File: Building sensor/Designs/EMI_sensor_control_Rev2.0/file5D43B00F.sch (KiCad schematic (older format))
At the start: 45 parts, among them U14 AD8021ARZ, U15 AD7763BSVZ

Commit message: overdue backup
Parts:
- removed C44, C52, C53, C54, C55, C56, C57, C58, C60, C61: C 100n, Capacitor_SMD:C_0603_1608Metric_Pad1.05x0.95mm_HandSolder, symbol Device:C
- removed C45: C 33p, Capacitor_SMD:C_0402_1005Metric, symbol Device:C
- removed C46: C 100u, Capacitor_Tantalum_SMD:CP_EIA-7343-30_AVX-N_Pad2.25x2.55mm_HandSolder, symbol Device:C
- removed C48, C59: C 10n, Capacitor_SMD:C_0805_2012Metric_Pad1.15x1.40mm_HandSolder, symbol Device:C
- removed FB11, FB12, FB13, FB14, FB15, FB16, FB17, FB18, FB19, FB20: Ferrite_Bead, Capacitor_SMD:C_0603_1608Metric_Pad1.05x0.95mm_HandSolder, symbol Device:Ferrite_Bead
- removed L6: L 8.2n, Inductor_SMD:L_0603_1608Metric_Pad1.05x0.95mm_HandSolder, symbol Device:L
- removed R49: R 10k, Resistor_SMD:R_1206_3216Metric_Pad1.42x1.75mm_HandSolder, symbol Device:R
- removed R51: R 100, Resistor_SMD:R_1206_3216Metric_Pad1.42x1.75mm_HandSolder, symbol Device:R
- removed R52: R 160k, Resistor_SMD:R_1206_3216Metric_Pad1.42x1.75mm_HandSolder, symbol Device:R
- removed R53, R61: R 10, Resistor_SMD:R_1206_3216Metric_Pad1.42x1.75mm_HandSolder, symbol Device:R
- removed R55, R56: R 18, Resistor_SMD:R_0805_2012Metric_Pad1.15x1.40mm_HandSolder, symbol Device:R
- removed U15: AD7763BSVZ, footprints:AD7763BSVZ, symbol 2019-07-11_15-43-26:AD7763BSVZ
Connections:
- net labels removed: +2V5, ADCReset, ADCSync, ADR0r, ADR1r, ADR2r, AGND1r, AGND2r, AGND3r, AGND4r, DRDY, FSI, FSOr, GNDD, GNDREF, GNDS, MCLK, Pin12r, Pin14r, Pin15r, Pin24r, Pin27r, Pin33r, Pin41r, Pin44r, Pin4r, Pin63r, Pin6r, SCO, SDI, SDLr, SDO, SH0r, SH1, SH2, Vref4.1
- wire segments 264 -> 51

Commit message: backup
2/04/2020
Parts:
- added C? (x7): C 1u, Capacitor_SMD:C_0402_1005Metric, symbol Device:C
- added R? (x3): R 100k, Resistor_SMD:R_0805_2012Metric_Pad1.15x1.40mm_HandSolder, symbol Device:R
- added R?: R 10k, Resistor_SMD:R_0805_2012Metric_Pad1.15x1.40mm_HandSolder, symbol Device:R
- added R?: R 60.4k, Resistor_SMD:R_0805_2012Metric_Pad1.15x1.40mm_HandSolder, symbol Device:R
- added U?: ADS127L01IPBSR, PBS0032A_N, symbol 2019-12-03_16-41-56:ADS127L01IPBSR
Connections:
- net GND: now also C?.1, C?.1, C?.1, C?.1, C?.1, C?.1, C?.2, R?.1, R?.1, R?.2, R?.2, U?.26 (DGND), U?.32 (AVDD), U?.5 (AGND)
- new net: C?.1, U?.1 (LVDD)
- new net: C?.2, U?.11 (CAP2)
- new net: R?.1, U?.14 (FSMODE)
- new net: C?.2, U?.2 (CAP1)
- new net: C?.2, U?.25 (CAP3)
- new net: R?.1, U?.29 (HR)
- new net: R?.1, U?.30 (FORMAT)
- new net: R?.2, U?.7 (REXT)
- new net: R?.2, U?.8 (INTLDO_N)
- new net +3V0: C?.2, C?.2, U?.27 (DVDD), U?.31 (AGND)
- new net +3V3: C?.2, R?.2, U?.6 (AVDD)
- new net Rx_CS: U?.19 (DRDY_FSYNC_N)
- new net Rx_Clk: U?.22 (SCLK)
- new net Rx_FIL0: U?.13 (FILTER0)
- new net Rx_FIL1: U?.12 (FILTER1)
- new net Rx_MISO: U?.20 (DOUT)
- new net Rx_MOSI: U?.21 (DIN)
- new net Rx_OSR0: U?.16 (OSR0)
- new net Rx_OSR1: U?.15 (OSR1)

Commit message: Back up
Backup of rev 2.0 for board
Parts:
- removed C49: C 5.6p, Capacitor_SMD:C_0402_1005Metric, symbol Device:C
- removed C50, C51: C 33p, Capacitor_SMD:C_0402_1005Metric, symbol Device:C
- removed R57, R58: R 1k, Resistor_SMD:R_0805_2012Metric_Pad1.15x1.40mm_HandSolder, symbol Device:R
- removed R59, R60: R 649, Resistor_SMD:R_0805_2012Metric_Pad1.15x1.40mm_HandSolder, symbol Device:R
- added R? (x2): R 1k, Resistor_SMD:R_0805_2012Metric_Pad1.15x1.40mm_HandSolder, symbol Device:R
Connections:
- net ADC_Reset: now also U?.28 (RESET_PWDN_N)
- net RxFiltered: now also R?.2
- net Rx_START: now also U?.17 (START)
- net -RxFiltered: now reaches R54.1, U14.6 (VOUT)
- net -RxFiltered: now also R?.2
- net at U?.3 (AINN): now also R?.1
- net at U?.4 (AINP): now also R?.1
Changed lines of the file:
@@
 $EndDescr
-$Comp
-L Device:R R58
-U 1 1 5D456184
-P 6350 9850
-AR Path="/5D3E2E6F/5D43B010/5D456184" Ref="R58"  Part="1"
-AR Path="/5DB20FE4/5D456184" Ref="R?"  Part="1"
-F 0 "R58" V 6350 9850 50  0000 C CNN
-F 1 "R 1k" V 6234 9850 50  0000 C CNN
-F 2 "Resistor_SMD:R_0805_2012Metric_Pad1.15x1.40mm_HandSolder" V 6280 9850 50  0001 C CNN
-F 3 "~" H 6350 9850 50  0001 C CNN
-	1    6350 9850
-	0    1    1    0
-$EndComp
 $Comp
 L Device:R R48
@@
 	5800 9650 5800 9550
 Connection ~ 5800 9650
-$Comp
-L Device:C C49
-U 1 1 5D4561C9
-P 6750 9650
-AR Path="/5D3E2E6F/5D43B010/5D4561C9" Ref="C49"  Part="1"
-AR Path="/5DB20FE4/5D4561C9" Ref="C?"  Part="1"
-F 0 "C49" H 6865 9696 50  0000 L CNN
-F 1 "C 5.6p" H 6800 9550 50  0000 L CNN
-F 2 "Capacitor_SMD:C_0402_1005Metric" H 6788 9500 50  0001 C CNN
-F 3 "~" H 6750 9650 50  0001 C CNN
-	1    6750 9650
-	1    0    0    -1
-$EndComp
-Wire Wire Line
-	6750 9500 6750 9450
-$Comp
-L Device:R R57
-U 1 1 5D4561D0
-P 6350 9450
-AR Path="/5D3E2E6F/5D43B010/5D4561D0" Ref="R57"  Part="1"
-AR Path="/5DB20FE4/5D4561D0" Ref="R?"  Part="1"
-F 0 "R57" V 6350 9450 50  0000 C CNN
-F 1 "R 1k" V 6234 9450 50  0000 C CNN
-F 2 "Resistor_SMD:R_0805_2012Metric_Pad1.15x1.40mm_HandSolder" V 6280 9450 50  0001 C CNN
-F 3 "~" H 6350 9450 50  0001 C CNN
-	1    6350 9450
-	0    1    1    0
-$EndComp
-Wire Wire Line
-	6500 9850 6750 9850
-Wire Wire Line
-	6500 9450 6750 9450
-Wire Wire Line
-	6750 9850 6750 9800
-Text GLabel 7100 9850 2    50   Input ~ 0
-Pin20r
-Text GLabel 7100 9450 2    50   Input ~ 0
-Pin19r
-Wire Wire Line
-	6750 9850 7100 9850
-Connection ~ 6750 9850
-Wire Wire Line
-	6750 9450 7100 9450
-Connection ~ 6750 9450
-Text GLabel 7700 10000 2    50   Input ~ 0
-Pin22r+
-Text GLabel 7700 9300 2    50   Input ~ 0
-Pin21r-
-Connection ~ 5950 9850
-Wire Wire Line
-	5950 9850 6200 9850
 Wire Wire Line
 	4600 9150 5950 9150
-$Comp
-L Device:R R59
-U 1 1 5D4561F0
-P 7050 9200
-AR Path="/5D3E2E6F/5D43B010/5D4561F0" Ref="R59"  Part="1"
-AR Path="/5DB20FE4/5D4561F0" Ref="R?"  Part="1"
-F 0 "R59" V 7050 9200 50  0000 C CNN
-F 1 "R 649" V 6934 9200 50  0000 C CNN
-F 2 "Resistor_SMD:R_0805_2012Metric_Pad1.15x1.40mm_HandSolder" V 6980 9200 50  0001 C CNN
-F 3 "~" H 7050 9200 50  0001 C CNN
-	1    7050 9200
-	0    1    1    0
-$EndComp
-$Comp
-L Device:C C51
-U 1 1 5D4561F6
-P 7050 10350
-AR Path="/5D3E2E6F/5D43B010/5D4561F6" Ref="C51"  Part="1"
-AR Path="/5DB20FE4/5D4561F6" Ref="C?"  Part="1"
-F 0 "C51" V 7300 10300 50  0000 L CNN
-F 1 "C 33p" V 7200 10200 50  0000 L CNN
-F 2 "Capacitor_SMD:C_0402_1005Metric" H 7088 10200 50  0001 C CNN
-F 3 "~" H 7050 10350 50  0001 C CNN
-	1    7050 10350
-	0    1    1    0
-$EndComp
-$Comp
-L Device:C C50
-U 1 1 5D4561FC
-P 7050 8850
-AR Path="/5D3E2E6F/5D43B010/5D4561FC" Ref="C50"  Part="1"
-AR Path="/5DB20FE4/5D4561FC" Ref="C?"  Part="1"
-F 0 "C50" V 6800 8800 50  0000 L CNN
-F 1 "C 33p" V 6900 8750 50  0000 L CNN
-F 2 "Capacitor_SMD:C_0402_1005Metric" H 7088 8700 50  0001 C CNN
-F 3 "~" H 7050 8850 50  0001 C CNN
-	1    7050 8850
-	0    1    1    0
-$EndComp
-Wire Wire Line
-	6750 9450 6750 9200
-Wire Wire Line
-	6750 8850 6900 8850
-Wire Wire Line
-	6900 9200 6750 9200
-Connection ~ 6750 9200
-Wire Wire Line
-	6750 9200 6750 8850
-Wire Wire Line
-	7200 9200 7550 9200
-Wire Wire Line
-	7550 9200 7550 9300
-Wire Wire Line
-	7550 9300 7700 9300
-Wire Wire Line
-	7200 8850 7550 8850
-Wire Wire Line
-	7550 8850 7550 9200
-Connection ~ 7550 9200
-Wire Wire Line
-	6750 9850 6750 10150
-Wire Wire Line
-	6750 10150 6900 10150
-Wire Wire Line
-	6750 10150 6750 10350
-Wire Wire Line
-	6750 10350 6900 10350
-Connection ~ 6750 10150
-Wire Wire Line
-	7200 10350 7550 10350
-Wire Wire Line
-	7550 10350 7550 10150
-Wire Wire Line
-	7550 10000 7700 10000
-Wire Wire Line
-	7200 10150 7550 10150
-Connection ~ 7550 10150
-Wire Wire Line
-	7550 10150 7550 10000
-Text GLabel 6050 9300 1    50   Input ~ 0
-RxFiltered
-Wire Wire Line
-	6050 9300 6050 9450
-Wire Wire Line
-	6050 9450 6200 9450
 $Comp
 L power:GND #PWR094
@@
 $EndComp
 $Comp
-L Device:R R60
-U 1 1 5D4561EA
-P 7050 10150
-AR Path="/5D3E2E6F/5D43B010/5D4561EA" Ref="R60"  Part="1"
-AR Path="/5DB20FE4/5D4561EA" Ref="R?"  Part="1"
-F 0 "R60" V 7050 10150 50  0000 C CNN
-F 1 "R 649" V 6934 10150 50  0000 C CNN
-F 2 "Resistor_SMD:R_0805_2012Metric_Pad1.15x1.40mm_HandSolder" V 6980 10150 50  0001 C CNN
-F 3 "~" H 7050 10150 50  0001 C CNN
-	1    7050 10150
-	0    1    1    0
-$EndComp
-$Comp
 L 2019-12-03_16-41-56:ADS127L01IPBSR U?
 U 1 1 5DF15BD4
@@
 Text GLabel 9000 5350 2    50   Input ~ 0
 Rx_FIL0
-Text GLabel 9000 4800 2    50   Input ~ 0
+Text GLabel 9000 4850 2    50   Input ~ 0
 Rx_START
-Text GLabel 9000 4700 2    50   Input ~ 0
+Text GLabel 9000 4750 2    50   Input ~ 0
 ADC_Reset
 Wire Wire Line
-	9000 4700 8750 4700
-Wire Wire Line
-	8750 4800 9000 4800
+	9000 4750 8750 4750
+Wire Wire Line
+	8750 4850 9000 4850
 Wire Wire Line
 	9000 5050 8750 5050
@@
 Connection ~ 5900 3050
 Connection ~ 6350 3350
+$Comp
+L Device:R R?
+U 1 1 5F3E958D
+P 6550 4300
+AR Path="/5D3E2E6F/5D43B010/5F3E958D" Ref="R?"  Part="1"
+AR Path="/5DB20FE4/5F3E958D" Ref="R?"  Part="1"
+F 0 "R?" V 6550 4300 50  0000 C CNN
+F 1 "R 1k" V 6434 4300 50  0000 C CNN
+F 2 "Resistor_SMD:R_0805_2012Metric_Pad1.15x1.40mm_HandSolder" V 6480 4300 50  0001 C CNN
+F 3 "~" H 6550 4300 50  0001 C CNN
+	1    6550 4300
+	0    1    1    0
+$EndComp
+Wire Wire Line
+	6700 4300 6950 4300
+Text GLabel 6250 4300 0    50   Input ~ 0
+RxFiltered
+Wire Wire Line
+	6250 4300 6400 4300
+$Comp
+L Device:R R?
+U 1 1 5F3EE38F
+P 6550 4400
+AR Path="/5D3E2E6F/5D43B010/5F3EE38F" Ref="R?"  Part="1"
+AR Path="/5DB20FE4/5F3EE38F" Ref="R?"  Part="1"
+F 0 "R?" V 6550 4400 50  0000 C CNN
+F 1 "R 1k" V 6650 4400 50  0000 C CNN
+F 2 "Resistor_SMD:R_0805_2012Metric_Pad1.15x1.40mm_HandSolder" V 6480 4400 50  0001 C CNN
+F 3 "~" H 6550 4400 50  0001 C CNN
+	1    6550 4400
+	0    1    1    0
+$EndComp
+Wire Wire Line
+	6700 4400 6950 4400
+Text GLabel 6250 4400 0    50   Input ~ 0
+-RxFiltered
+Wire Wire Line
+	6250 4400 6400 4400
+Text GLabel 6150 9850 2    50   Input ~ 0
+-RxFiltered
+Wire Wire Line
+	6150 9850 5950 9850
+Connection ~ 5950 9850
 $EndSCHEMATC

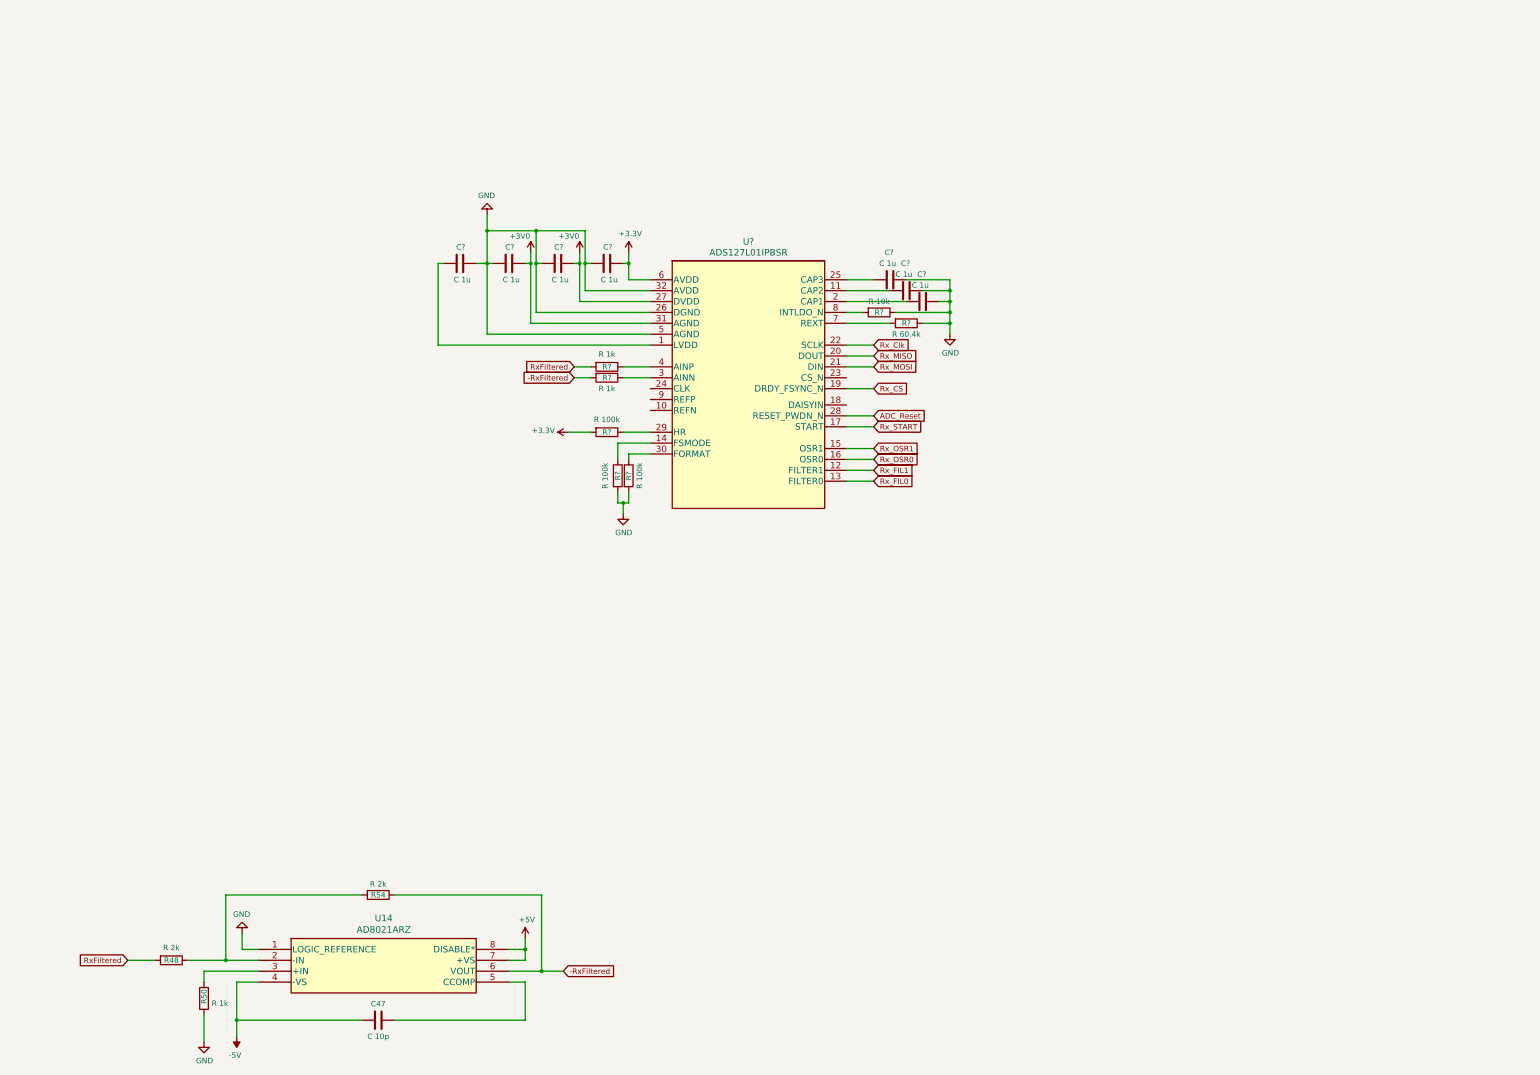
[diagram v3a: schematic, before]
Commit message: Rev 2.0 Complete
Rev 2.0 of PCB Completed
SCHM, PCB layout, and gerber files generated
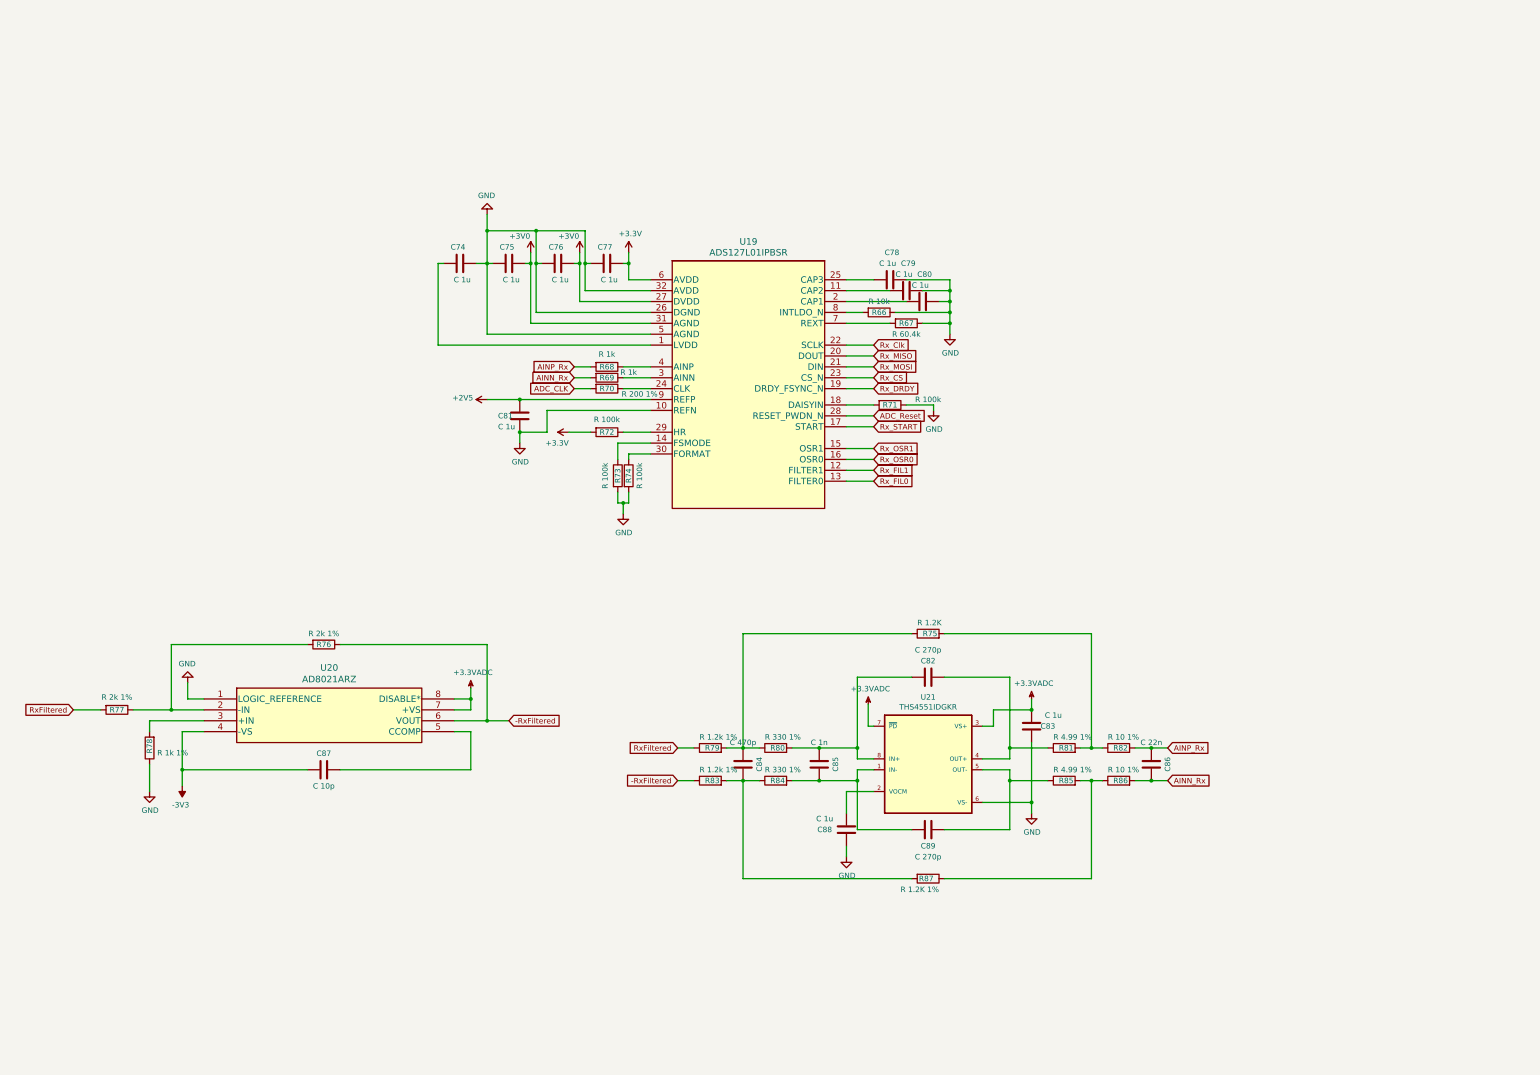
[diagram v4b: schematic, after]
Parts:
- removed R? (x2): R 1k, Resistor_SMD:R_0805_2012Metric_Pad1.15x1.40mm_HandSolder, symbol Device:R
- added C81, C83, C88: C 1u, Capacitor_SMD:C_0805_2012Metric_Pad1.15x1.40mm_HandSolder, symbol Device:C
- added C82, C89: C 270p, Capacitor_SMD:C_0805_2012Metric_Pad1.15x1.40mm_HandSolder, symbol Device:C
- added C84: C 470p, Capacitor_SMD:C_0603_1608Metric_Pad1.05x0.95mm_HandSolder, symbol Device:C
- added C85: C 1n, Capacitor_SMD:C_0603_1608Metric_Pad1.05x0.95mm_HandSolder, symbol Device:C
- added C86: C 22n, Capacitor_SMD:C_0805_2012Metric_Pad1.15x1.40mm_HandSolder, symbol Device:C
- added R68, R69: R 1k, Resistor_SMD:R_0805_2012Metric_Pad1.15x1.40mm_HandSolder, symbol Device:R
- added R70: R 200 1%, Resistor_SMD:R_0805_2012Metric_Pad1.15x1.40mm_HandSolder, symbol Device:R
- added R71: R 100k, Resistor_SMD:R_0805_2012Metric_Pad1.15x1.40mm_HandSolder, symbol Device:R
- added R75: R 1.2K, Resistor_SMD:R_0805_2012Metric_Pad1.15x1.40mm_HandSolder, symbol Device:R
- added R79, R83: R 1.2k 1%, Resistor_SMD:R_0805_2012Metric_Pad1.15x1.40mm_HandSolder, symbol Device:R
- added R80, R84: R 330 1%, Resistor_SMD:R_0805_2012Metric_Pad1.15x1.40mm_HandSolder, symbol Device:R
- added R81, R85: R 4.99 1%, Resistor_SMD:R_0805_2012Metric_Pad1.15x1.40mm_HandSolder, symbol Device:R
- added R82, R86: R 10 1%, Resistor_SMD:R_0805_2012Metric_Pad1.15x1.40mm_HandSolder, symbol Device:R
- added R87: R 1.2K 1%, Resistor_SMD:R_0805_2012Metric_Pad1.15x1.40mm_HandSolder, symbol Device:R
- added U21: THS4551IDGKR, Package_SO:VSSOP-8_3.0x3.0mm_P0.65mm, symbol THS4551IDGKR:THS4551IDGKR
- C74, C75, C76, C77, C78, C79, C80: renamed from C?; footprint Capacitor_SMD:C_0402_1005Metric -> Capacitor_SMD:C_0805_2012Metric_Pad1.15x1.40mm_HandSolder
- C87: renamed from C47; footprint Capacitor_SMD:C_0805_2012Metric_Pad1.15x1.40mm_HandSolder -> Capacitor_SMD:C_0603_1608Metric_Pad1.05x0.95mm_HandSolder
- R76: renamed from R54; value R 2k -> R 2k 1%
- R77: renamed from R48; value R 2k -> R 2k 1%
- R78: renamed from R50; value R 1k -> R 1k 1%
- U19: renamed from U?; footprint PBS0032A_N -> SamacSys_Parts:QFP50P700X700X120-32N
- U20: renamed from U14; footprint footprints:AD8021ARZ -> Package_SO:SOIC-8_3.9x4.9mm_P1.27mm
- gave numbers to parts that had none: 5
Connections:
- net -RxFiltered: now also R83.1
- net GND: now also U19.10 (REFN), C81.2, C83.1, C88.1, R71.1, U21.6 (VS-)
- net RxFiltered: now also R79.1
- net Rx_CS: now also U19.23 (CS_N); no longer U19.19 (DRDY_FSYNC_N)
- net at U19.18 (DAISYIN): now also R71.2
- net at U19.24 (CLK): now also R70.1
- net at U19.3 (AINN): now also R69.1
- net at U19.4 (AINP): now also R68.1
- net +2V5: now reaches U19.9 (REFP)
- net +2V5: now also C81.1
- net +5V renamed +3.3VADC
- net +3.3VADC: now also C83.2, U21.3 (VS+), U21.7 (~PD~)
- net -5V renamed -3V3
- new net: C85.1, C89.1, R84.2, U21.1 (IN-)
- new net: C88.2, U21.2 (VOCM)
- new net: C82.1, R81.1, U21.4 (OUT+)
- new net: C89.2, R85.1, U21.5 (OUT-)
- new net: C82.2, C85.2, R80.2, U21.8 (IN+)
- new net: C84.2, R75.1, R79.2, R80.1
- new net: C84.1, R83.2, R84.1, R87.2
- new net: R75.2, R81.2, R82.1
- new net: R85.2, R86.1, R87.1
- new net ADC_CLK: R70.2
- new net AINN_Rx: C86.1, R69.2, R86.2
- new net AINP_Rx: C86.2, R68.2, R82.2
- new net Rx_DRDY: U19.19 (DRDY_FSYNC_N)
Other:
- moved on the sheet: C87, R76, R77, R78, U20
